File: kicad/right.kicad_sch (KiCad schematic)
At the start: 118 parts, among them Q1 PMF170XP,115, Q2 FS8205A_C2830320, SW1 TS-1088-AR02016, U1 TLV7031QDCKRQ1, U2 E73-2G4M08S1C, U3 SN74LVC1G74DQER, U4 BL8573CS8TR, U6 S2B-PH-K-S(LF)(SN), U7 LP5024RSMR, U8 DW01A_C42380662, X1 FC-13532.768KHZ9PF20PPM

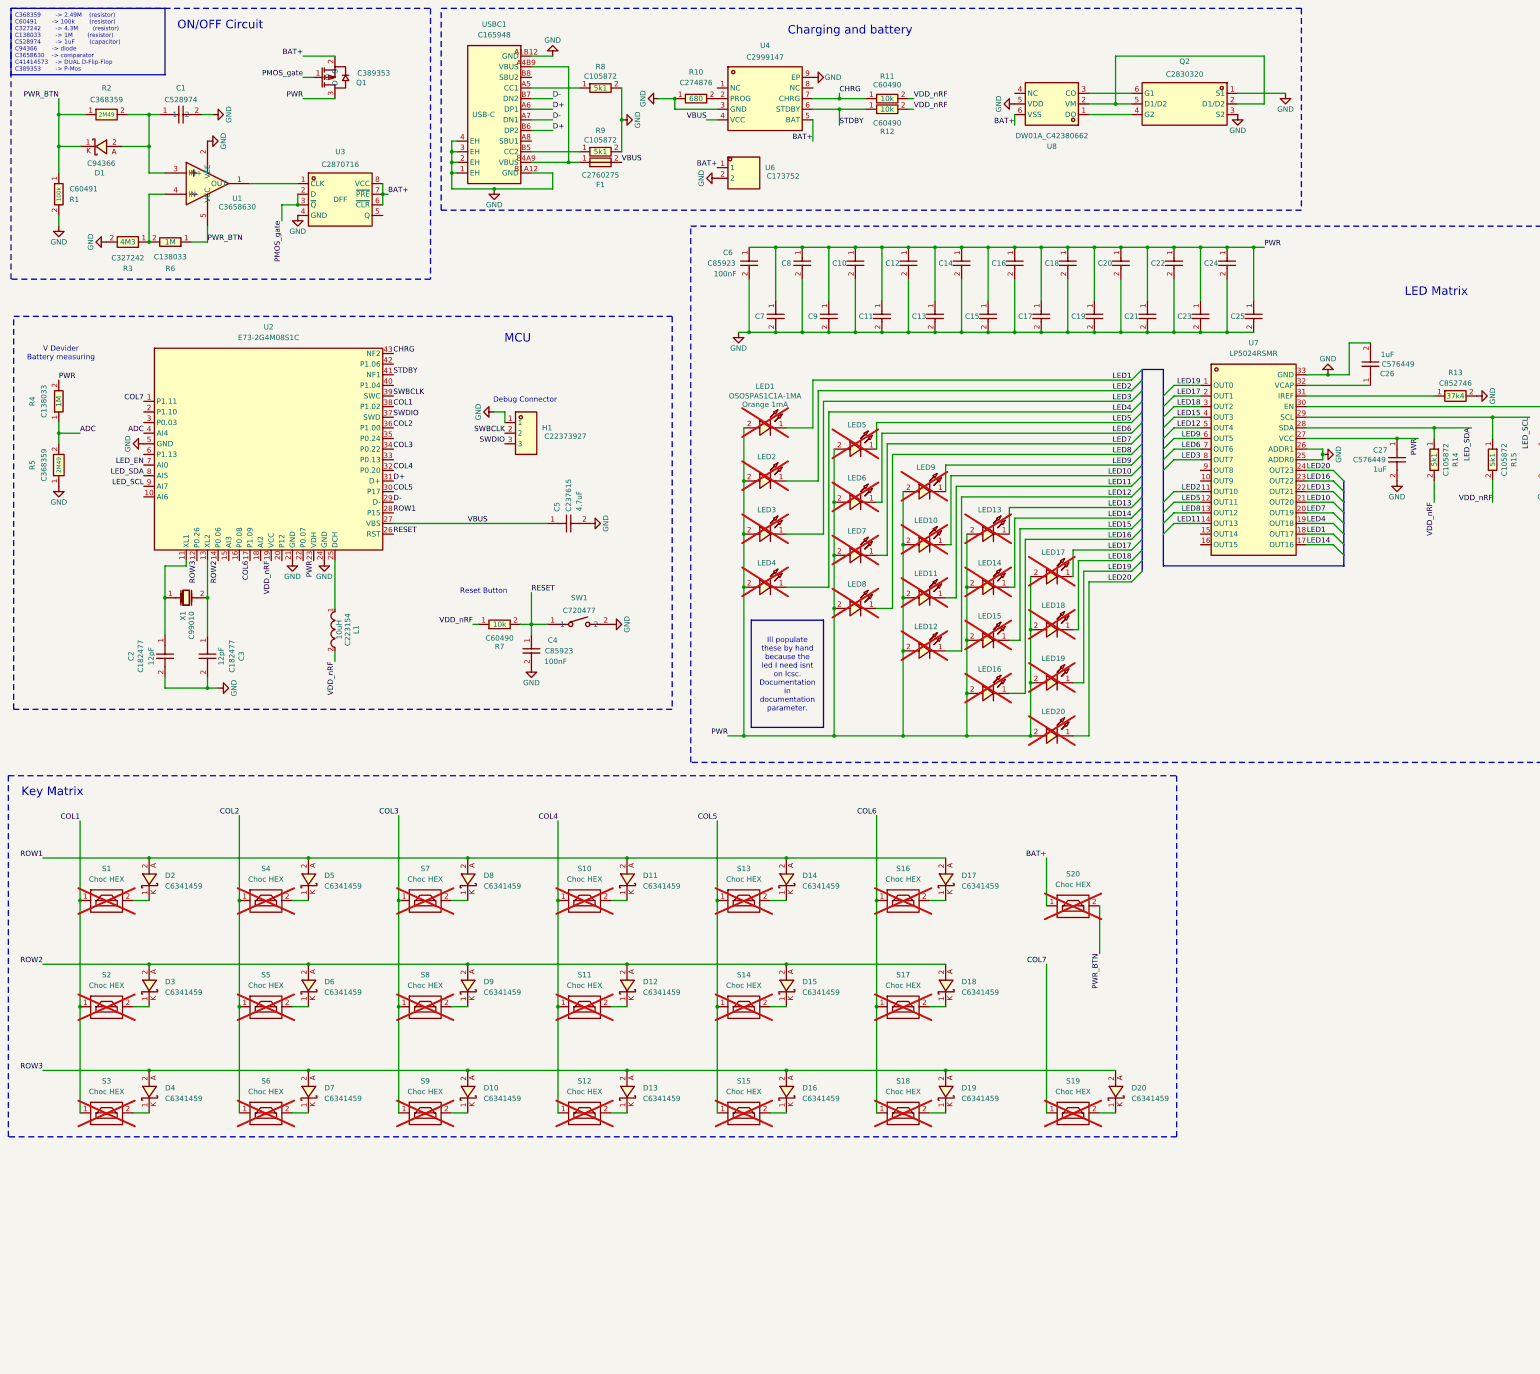
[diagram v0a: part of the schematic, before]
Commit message: integrated the move from distant index to lowest index... changed from 7colX3row to 5colX4row
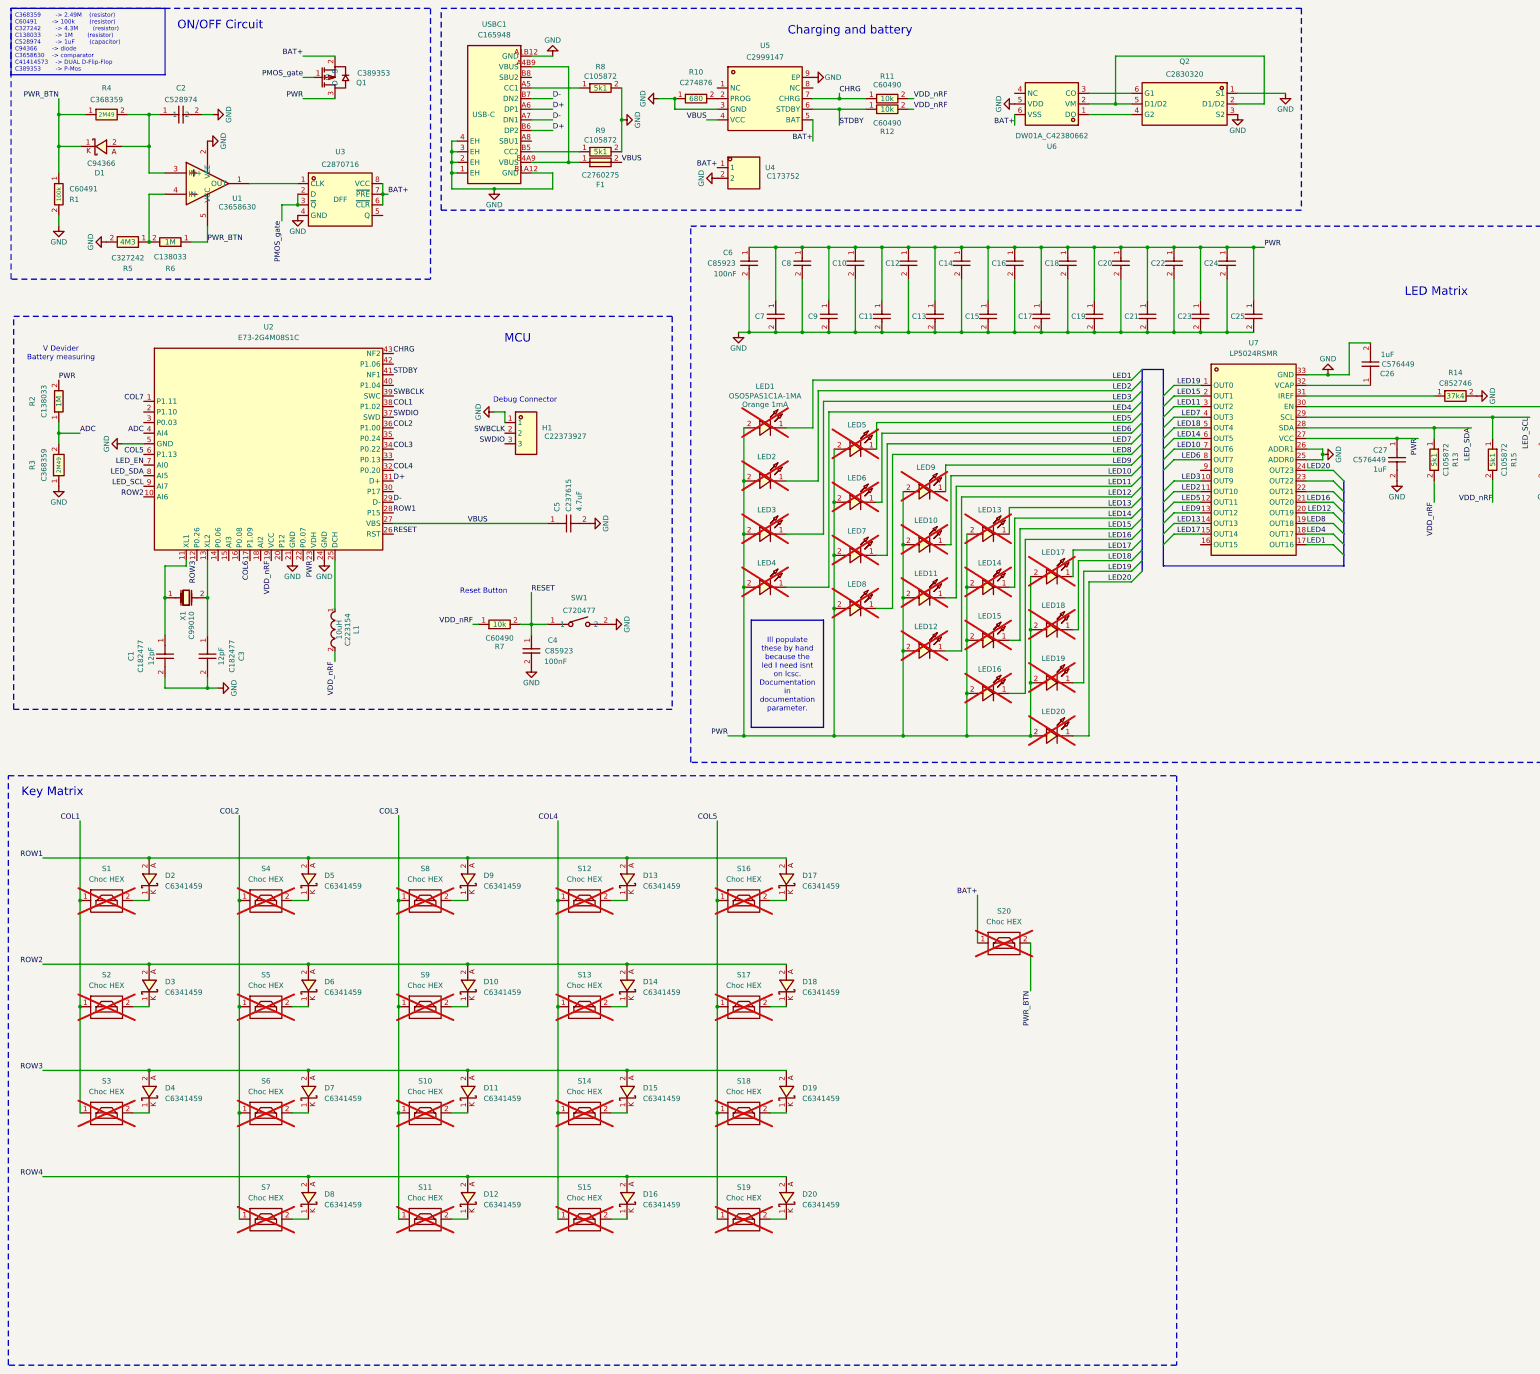
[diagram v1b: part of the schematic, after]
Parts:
- renumbered C2 to C1, C1 to C2, D9 to D10, D10 to D11, D18 to D12, D11 to D13, D12 to D14, D13 to D15, D19 to D16, D14 to D17, D15 to D18, D16 to D19, D17 to D8, D8 to D9, R14 to R13, R13 to R14, R4 to R2, R5 to R3, R2 to R4, R3 to R5, S9 to S10, S17 to S11, S10 to S12, S11 to S13, S12 to S14, S18 to S15, S13 to S16, S14 to S17, S15 to S18, S16 to S7, S7 to S8, S8 to S9, U6 to U4, U4 to U5, U8 to U6
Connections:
- net COL2: now also S7.1
- net COL3: now also S11.1
- net COL4: now also S15.1
- net COL5: now also S19.1, U2.6 (P1.13); no longer U2.30 (P17)
- net COL6: no longer S11.1, S15.1, S7.1
- net COL7: no longer S19.1
- net LED1: now also U7.17 (OUT16); no longer U7.18 (OUT17)
- net LED10: now also U7.7 (OUT6); no longer U7.21 (OUT20)
- net LED11: now also U7.3 (OUT2); no longer U7.14 (OUT13)
- net LED12: now also U7.20 (OUT19); no longer U7.5 (OUT4)
- net LED13: now also U7.14 (OUT13); no longer U7.22 (OUT21)
- net LED14: now also U7.6 (OUT5); no longer U7.17 (OUT16)
- net LED15: now also U7.2 (OUT1); no longer U7.4 (OUT3)
- net LED16: now also U7.21 (OUT20); no longer U7.23 (OUT22)
- net LED17: now also U7.15 (OUT14); no longer U7.2 (OUT1)
- net LED18: now also U7.5 (OUT4); no longer U7.3 (OUT2)
- net LED3: now also U7.10 (OUT9); no longer U7.8 (OUT7)
- net LED4: now also U7.18 (OUT17); no longer U7.19 (OUT18)
- net LED6: now also U7.8 (OUT7); no longer U7.7 (OUT6)
- net LED7: now also U7.4 (OUT3); no longer U7.20 (OUT19)
- net LED8: now also U7.19 (OUT18); no longer U7.13 (OUT12)
- net LED9: now also U7.13 (OUT12); no longer U7.6 (OUT5)
- net ROW1: no longer D8.2
- net ROW2: now also U2.10 (AI6); no longer D12.2, U2.14 (P0.06)
- net ROW3: no longer D16.2, D20.2
- new net ROW4: D12.2, D16.2, D20.2, D8.2
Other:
- moved on the sheet: D12, D16, D20, D8, S11, S15, S19, S20, S7

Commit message: ...
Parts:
- added R17: RC0402FR-071ML, easyeda2kicad:R0402, symbol easyeda2kicad:RC0402FR-071ML
- added R18: WR04W2494FTL, easyeda2kicad:R0402, symbol easyeda2kicad:WR04W2494FTL
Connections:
- net COL6 is gone; now on net LED_SCL: U2.17 (P1.09)
- net COL7 is gone; now on net SWBCLK: U2.1 (P1.11)
- net GND: now also R18.1
- net LED_EN: now also U2.15 (AI3); no longer U2.7 (AI0)
- net LED_SCL: no longer U2.9 (AI7)
- net LED_SDA: now also U2.16 (P0.08); no longer U2.8 (AI5)
- net PWR_BTN: now also R17.2
- net ROW4: now also U2.9 (AI7)
- net SWBCLK: no longer U2.39 (SWC)
- net SWDIO: now also U2.2 (P1.10); no longer U2.37 (SWD)
- net PWR_BTN_PRESS: now reaches U2.40 (P1.04)
- net PWR_BTN_PRESS: now also R17.1, R18.2
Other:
- moved on the sheet: H1

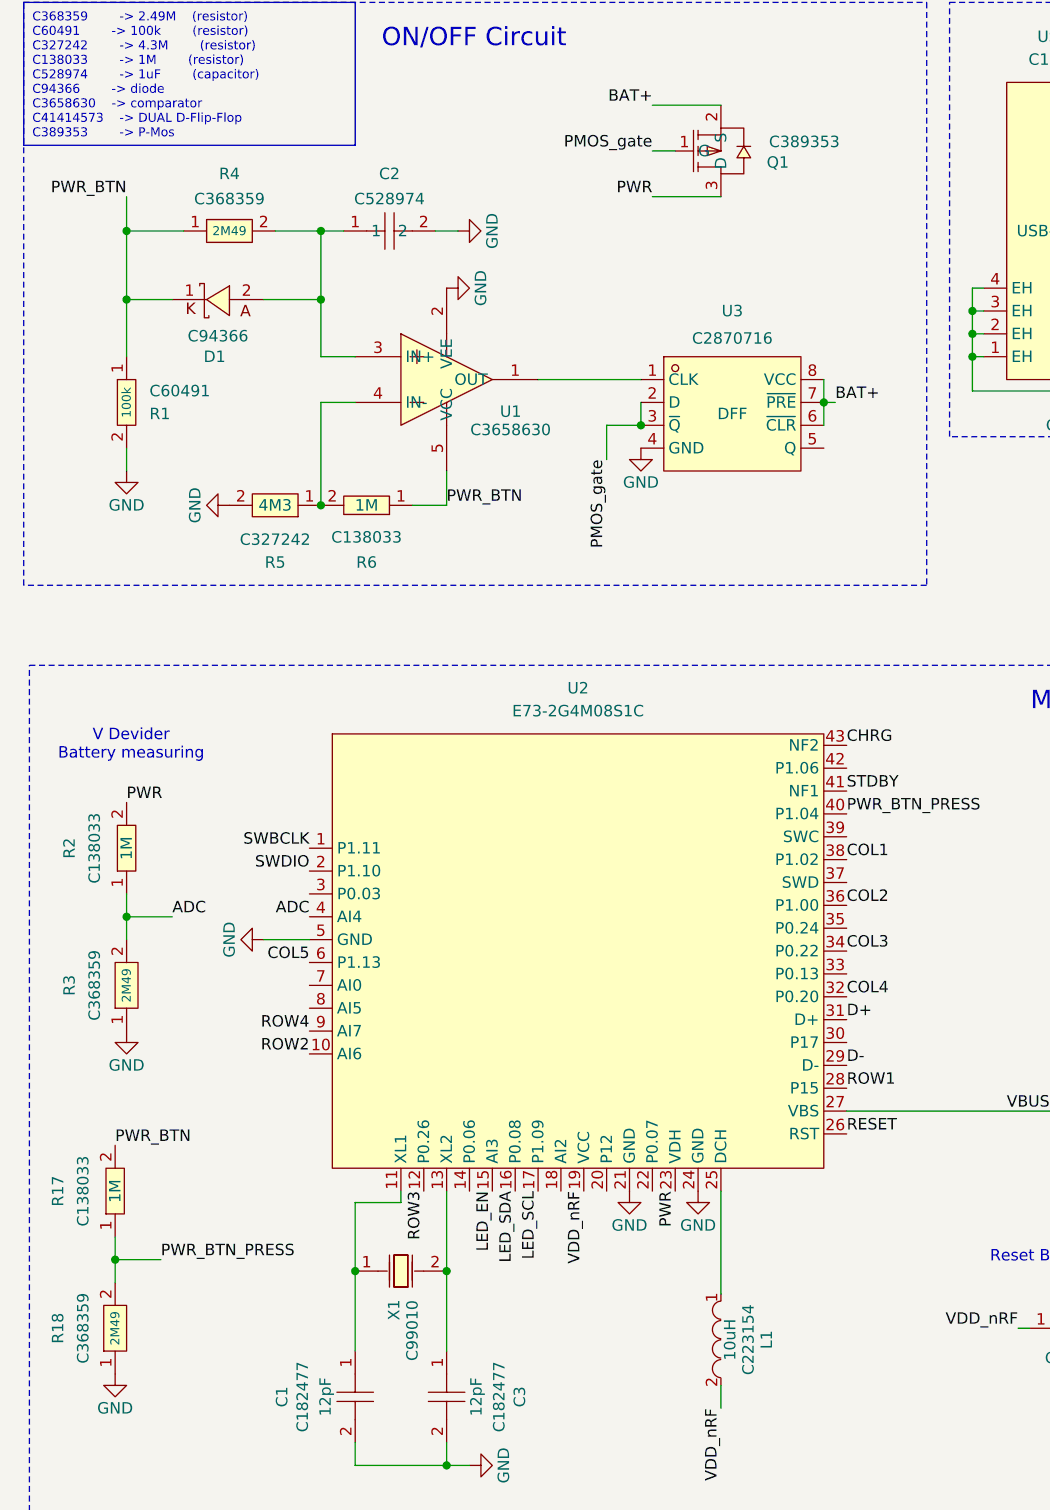
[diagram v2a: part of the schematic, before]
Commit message: left wiring done... right changed to shmitt inctead of comparator... need to do same on left... fixing of right in progress
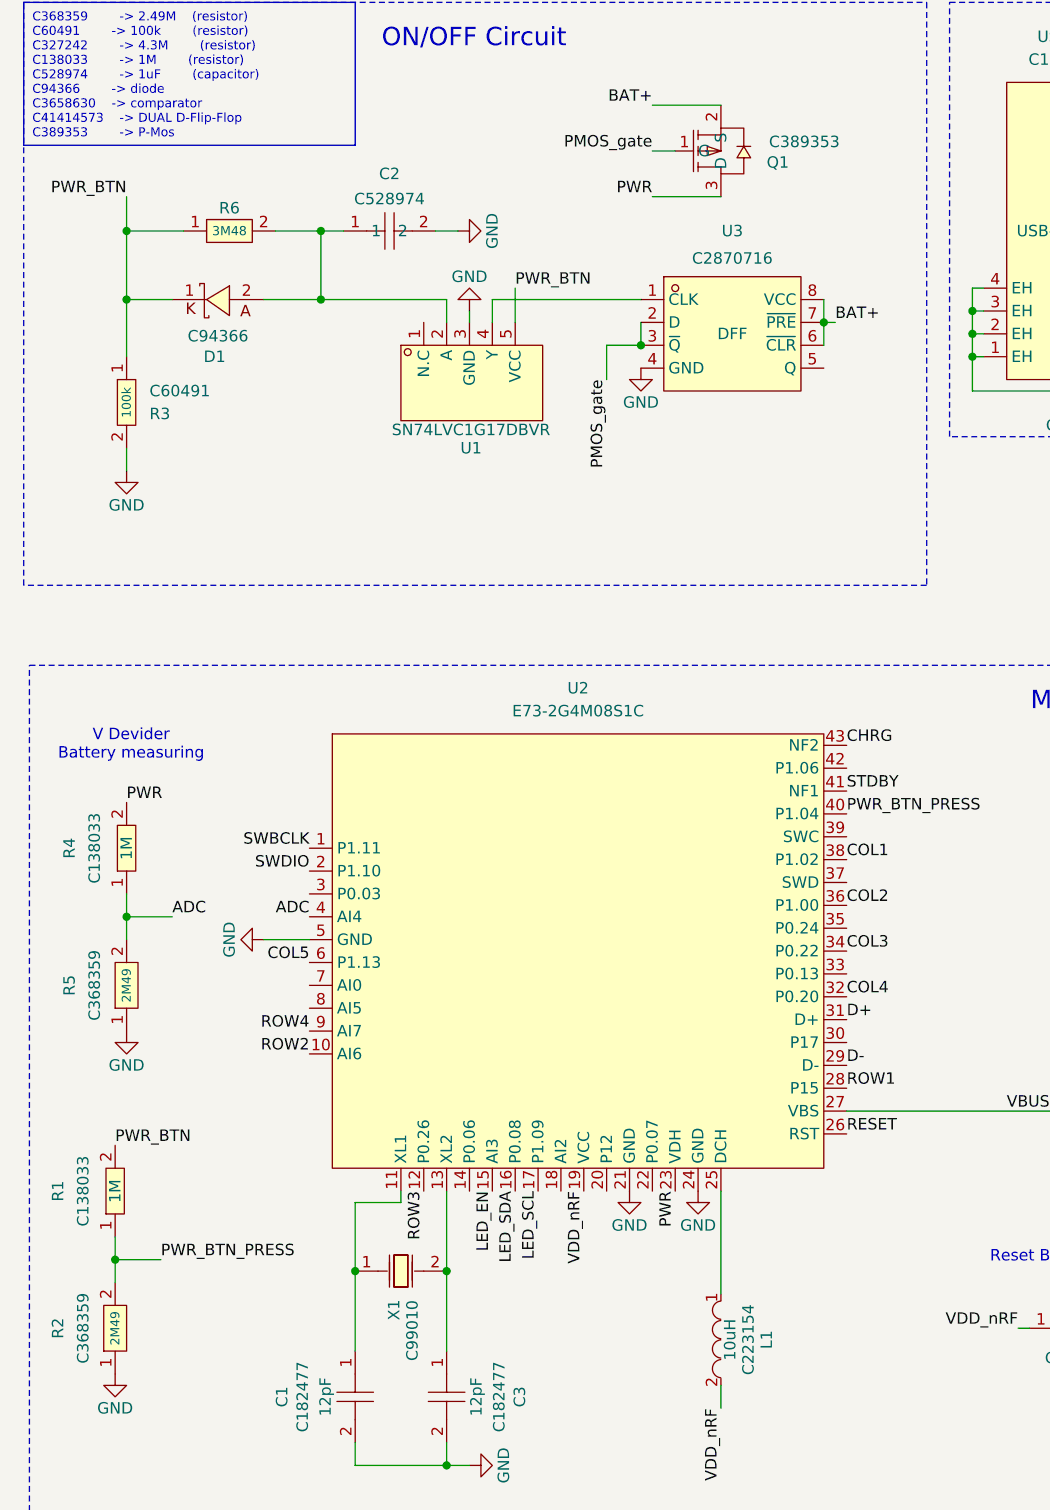
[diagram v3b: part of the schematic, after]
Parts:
- removed R4: WR04W2494FTL, easyeda2kicad:R0402, symbol easyeda2kicad:WR04W2494FTL
- removed R5: RC0402FR-074M3L, :R0402, symbol easyeda2kicad:RC0402FR-074M3L
- removed R6: RC0402FR-071ML, easyeda2kicad:R0402, symbol easyeda2kicad:RC0402FR-071ML
- removed U1: TLV7031QDCKRQ1, :SC-70-5_L2.0-W1.3-P0.65-LS2.1-BR, symbol easyeda2kicad:TLV7031QDCKRQ1
- added R6: 0402WGF1604TCE, easyeda2kicad:R0402, symbol easyeda2kicad:0402WGF1604TCE
- added U1: SN74LVC1G17DBVR, easyeda2kicad:SOT-23-5_L3.0-W1.7-P0.95-LS2.8-BR, symbol easyeda2kicad:SN74LVC1G17DBVR
- renumbered R17 to R1, R18 to R2, R1 to R3, R2 to R4, R3 to R5
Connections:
- net GND: now also U1.3 (GND)
- net PWR_BTN: now also R6.1, U1.5 (VCC)
- net at C2.1, D1.2: now also R6.2, U1.2 (A)
- net at U3.1 (CLK): now also U1.4 (Y)
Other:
- moved on the sheet: U3

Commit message: checked and update schematics on off need to update it in pcb...
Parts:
- added C4: GRM033C71C104KE14D, easyeda2kicad:C0201, symbol easyeda2kicad:GRM033C71C104KE14D
- added R7: RC0402FR-07100KL, easyeda2kicad:R0402, symbol easyeda2kicad:RC0402FR-07100KL
- renumbered C9 to C10, C10 to C11, C11 to C12, C12 to C13, C13 to C14, C14 to C15, C15 to C16, C16 to C17, C17 to C18, C18 to C19, C19 to C20, C20 to C21, C21 to C22, C22 to C23, C23 to C24, C24 to C25, C25 to C26, C26 to C27, C27 to C28, C4 to C5, C5 to C6, C6 to C7, C7 to C8, C8 to C9, R9 to R10, R10 to R11, R11 to R12, R12 to R13, R13 to R14, R14 to R15, R15 to R16, R16 to R17, R7 to R8, R8 to R9
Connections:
- net BAT+: now also U1.5 (VCC), R7.2; no longer U3.6 (~{CLR})
- net GND: now also C4.1
- net PWR_BTN: no longer U1.5 (VCC)
- new net: C4.2, R7.1, U3.6 (~{CLR})
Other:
- moved on the sheet: U1, U3

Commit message: started redesign... removed led caps and moved everything to fron layer... need to move debug connector to front and than try to change pcb stack.
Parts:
- removed C10, C11, C12, C13, C14, C15, C16, C17, C18, C19, C20, C21, C22, C23, C24, C25, C26, C7, C8, C9: GRM033C71C104KE14D, easyeda2kicad:C0201, symbol easyeda2kicad:GRM033C71C104KE14D
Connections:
- net CHRG: now also U2.41 (NF1); no longer U2.43 (NF2)
- net STDBY: now also U2.43 (NF2); no longer U2.41 (NF1)
- net SWBCLK: now also U2.39 (SWC); no longer U2.1 (P1.11)
- net SWDIO: now also U2.37 (SWD); no longer U2.2 (P1.10)

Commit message: .
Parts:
- removed C6: GRM188C71C475KE21D, easyeda2kicad:C0603, symbol easyeda2kicad:GRM188C71C475KE21D
- removed R7: RC0402FR-07100KL, easyeda2kicad:R0402, symbol easyeda2kicad:RC0402FR-07100KL
- added C5: ZRB15XR61A475KE01D, easyeda2kicad:C0402, symbol easyeda2kicad:ZRB15XR61A475KE01D
- added R7: RC0402FR-0710KL, easyeda2kicad:R0402, symbol easyeda2kicad:RC0402FR-0710KL
- renumbered C5 to C6, C27 to C7, C28 to C8
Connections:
- net BAT+: now also R7.2
- net GND: now also C5.2
- net PWR_BTN_PRESS: now also U2.30 (P17); no longer U2.40 (P1.04)
- net VBUS: now also C5.1
- net at C4.2, U3.6 (~{CLR}): now also R7.1
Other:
- moved on the sheet: C1, C2, C3, C4, C6, C7, C8, D1, D10, D11, D12, D13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

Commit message: .
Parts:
- removed R4: RC0402FR-071ML, easyeda2kicad:R0402, symbol easyeda2kicad:RC0402FR-071ML
- removed R5: WR04W2494FTL, easyeda2kicad:R0402, symbol easyeda2kicad:WR04W2494FTL
- added C9: GRM033C71C104KE14D, easyeda2kicad:C0201, symbol easyeda2kicad:GRM033C71C104KE14D
- added R4: RC0402FR-0710KL, easyeda2kicad:R0402, symbol easyeda2kicad:RC0402FR-0710KL
- added U8: MAX17048, PCM_SparkFun-Semiconductor-Standard:DFN-8_2x2mm_P0.5mm_EP1.2x0.8mm, symbol PCM_SparkFun-IC-Power:MAX17048
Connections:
- net BAT+: now also C9.1, U8.2 (CELL), U8.3 (VDD)
- net GND: now also C9.2, U8.1 (CTG), U8.4 (GND), U8.6 (QSTRT), U8.9 (GND)
- net LED20: now also U7.22 (OUT21); no longer U7.24 (OUT23)
- net VDD_nRF: now also R4.2
- net BAT_ALTR: now reaches U2.18 (AI2)
- net BAT_ALTR: now also R4.1, U8.5 (~{ALRT})
- net ADC: no longer names the net of U2.4 (AI4)
- net LED_SCL renamed SCL
- net SCL: now also U8.7 (SCL)
- net LED_SDA renamed SDA
- net SDA: now also U8.8 (SDA)
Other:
- moved on the sheet: F1, Q2, R10, R9, U4, U6, USBC1
